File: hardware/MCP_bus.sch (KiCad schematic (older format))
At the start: 165 parts, among them J5 GPIO_1, J6 GPIO_2, U13 TXB0108DQSR, U14 TXB0108DQSR, U15 TXB0108DQSR, U16 TXB0108DQSR, U17 TXB0108DQSR, U18 TXB0108DQSR, U19 TXB0108DQSR, U20 TXB0108DQSR, U4 EP4CE6F17

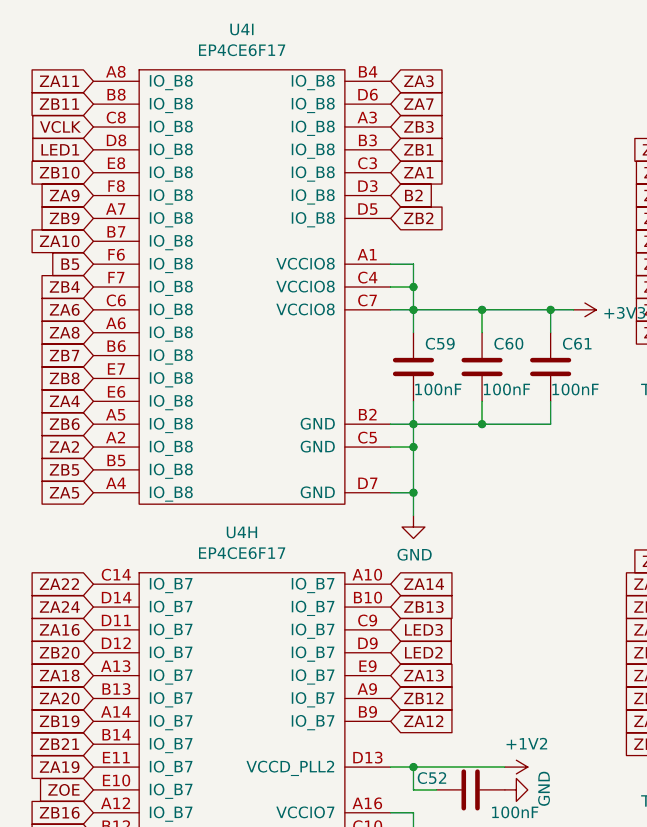
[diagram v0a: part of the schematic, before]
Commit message: Обновлена схема:
1. Исправлена нумерация CS SRAM;
2. Исправлена нумерация сигналов для светодиодов.
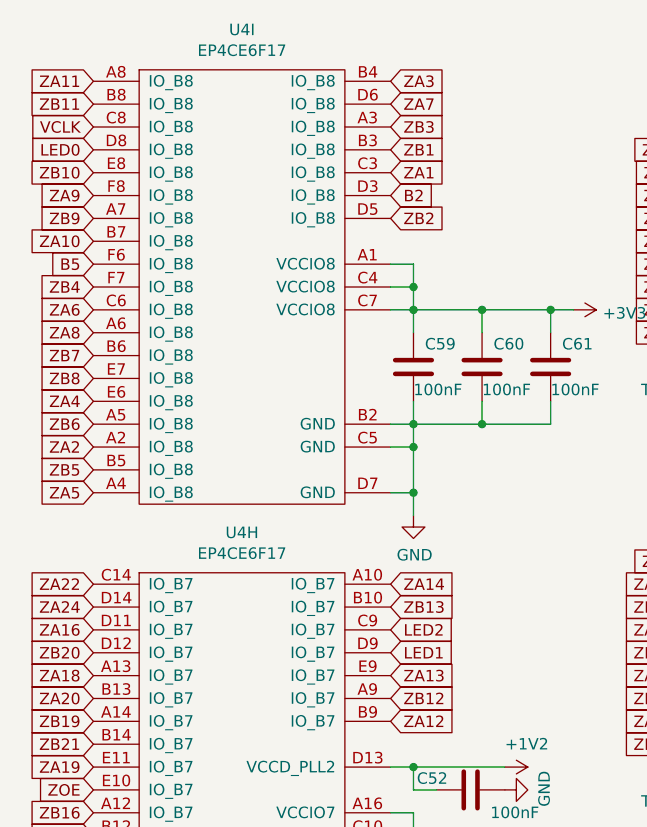
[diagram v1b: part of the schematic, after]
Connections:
- net LED3 is gone; now on net LED2: U4.C9 (IO_B7)
- net LED1: now also U4.D9 (IO_B7); no longer U4.D8 (IO_B8)
- net LED2: no longer U4.D9 (IO_B7)
- new net LED0: U4.D8 (IO_B8)
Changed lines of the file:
@@
 VCLK
 Text GLabel 900  1100 0    50   Input ~ 0
+LED0
+Text GLabel 2200 3300 2    50   Input ~ 0
 LED1
-Text GLabel 2200 3300 2    50   Input ~ 0
+Text GLabel 2200 3200 2    50   Input ~ 0
 LED2
-Text GLabel 2200 3200 2    50   Input ~ 0
-LED3
 $EndSCHEMATC
